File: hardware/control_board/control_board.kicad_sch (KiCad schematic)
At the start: 32 parts, among them J1 SWD, J2 Aux, J3 Panel, SW1 Reset, U1 STM32F103C8T6, Y1 8MHz

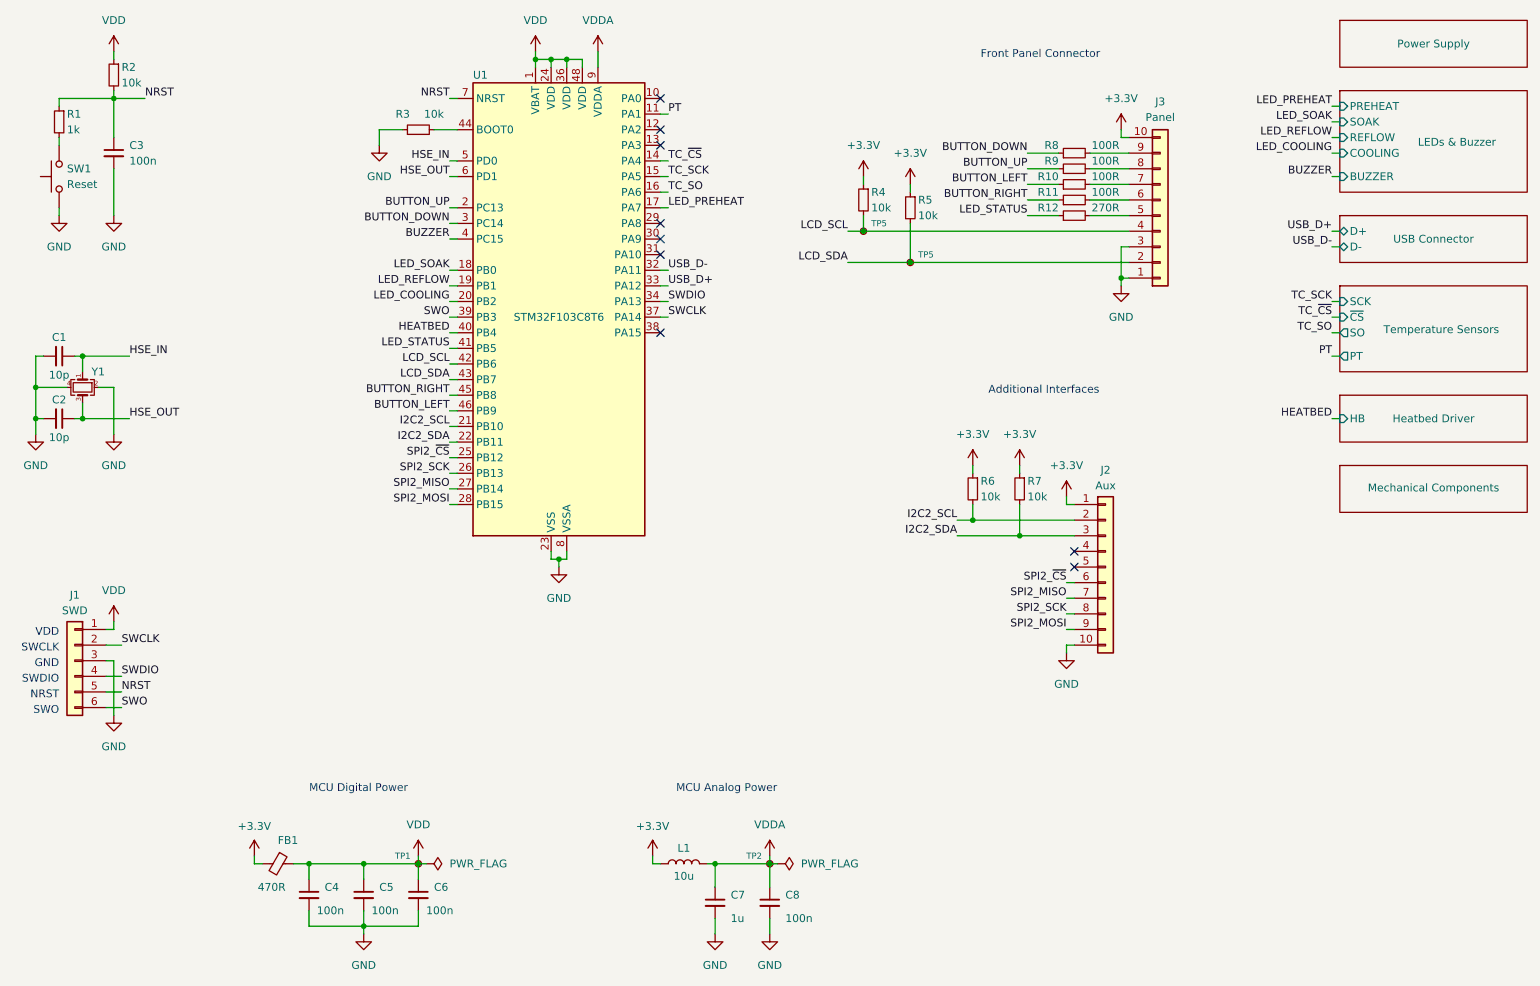
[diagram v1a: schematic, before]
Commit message: Change the buzzer
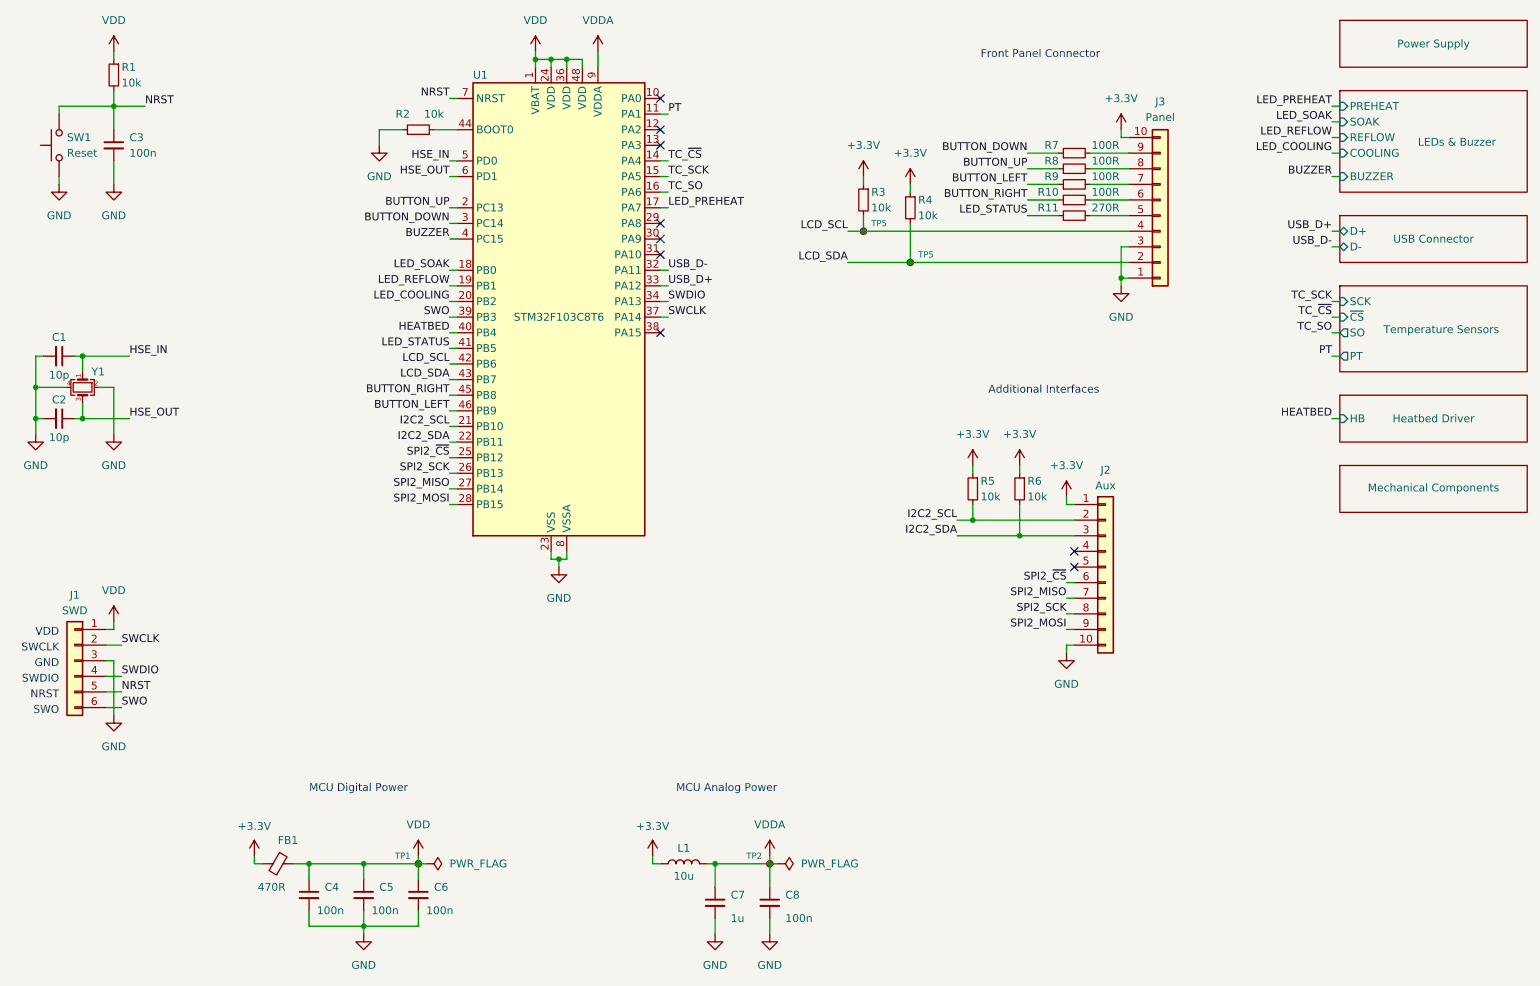
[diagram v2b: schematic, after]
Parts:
- removed R1: 1k, Resistor_SMD:R_0603_1608Metric, symbol Device:R_Small
- renumbered R2 to R1, R11 to R10, R12 to R11, R3 to R2, R4 to R3, R5 to R4, R6 to R5, R7 to R6, R8 to R7, R9 to R8, R10 to R9
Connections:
- net NRST: now also SW1.2
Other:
- moved on the sheet: C3, SW1

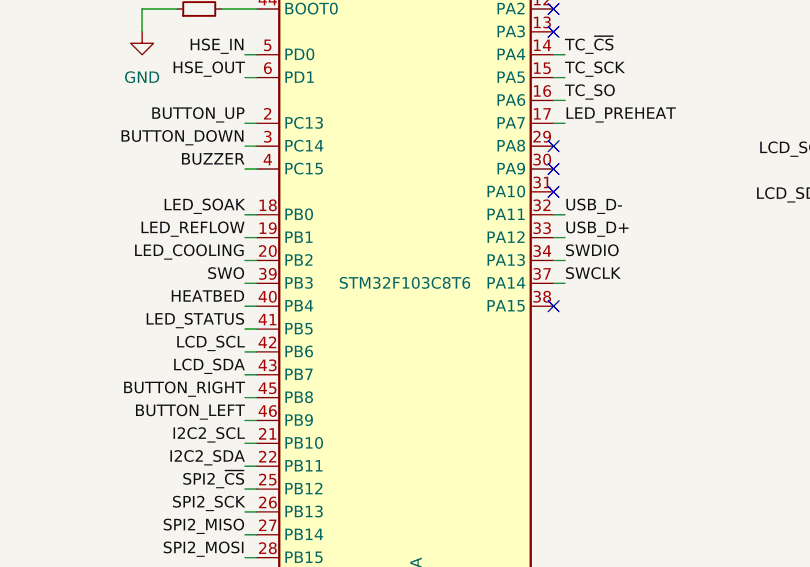
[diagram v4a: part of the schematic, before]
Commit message: Change MCU to STM32F103CBT6
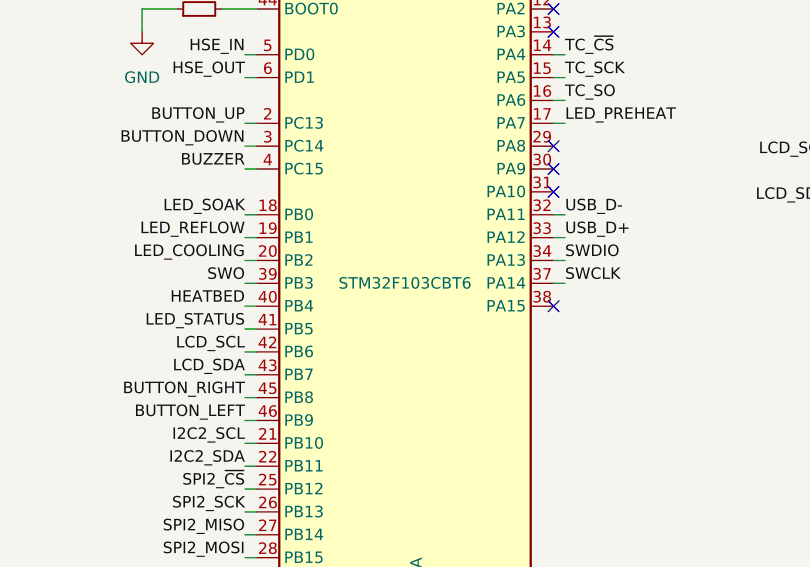
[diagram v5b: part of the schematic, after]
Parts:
- U1: value STM32F103C8T6 -> STM32F103CBT6
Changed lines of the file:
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@@
       (effects (font (size 1.27 1.27)) (justify left))
     )
-    (property "Value" "STM32F103C8T6" (at 114.3 78.74 0)
+    (property "Value" "STM32F103CBT6" (at 114.3 78.74 0)
       (effects (font (size 1.27 1.27)))
     )

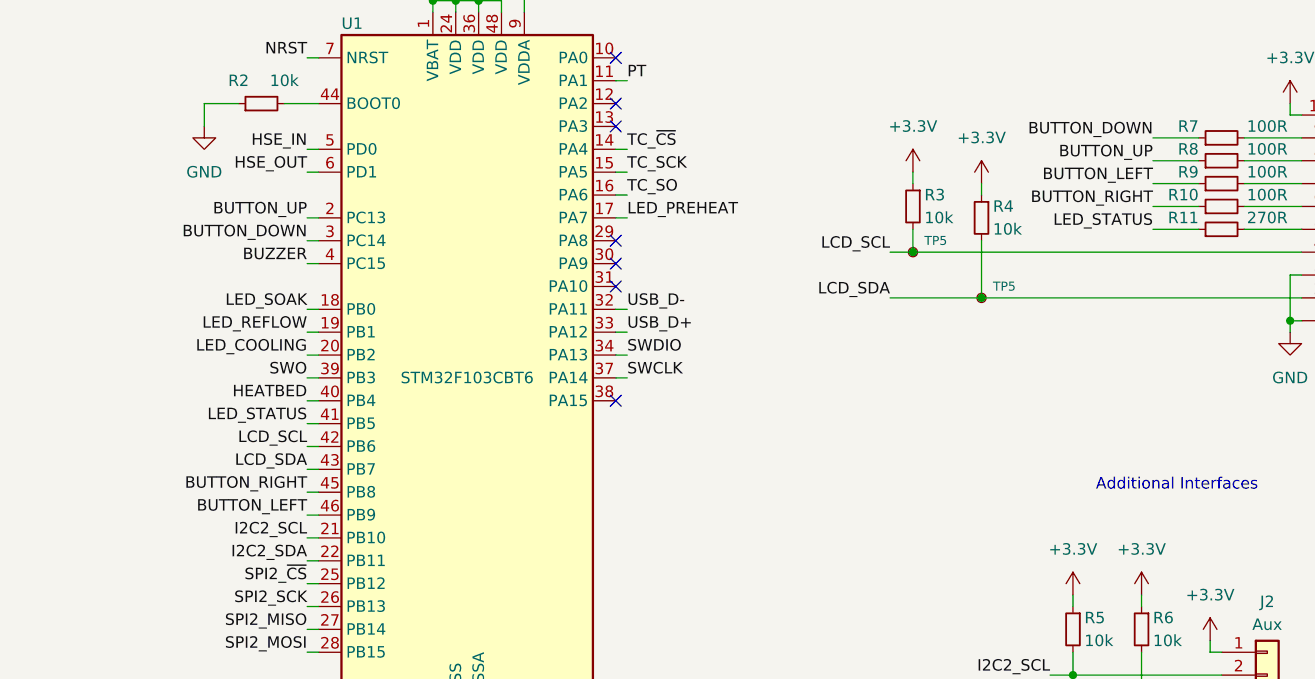
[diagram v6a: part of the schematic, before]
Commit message: Swap the left and right button signals
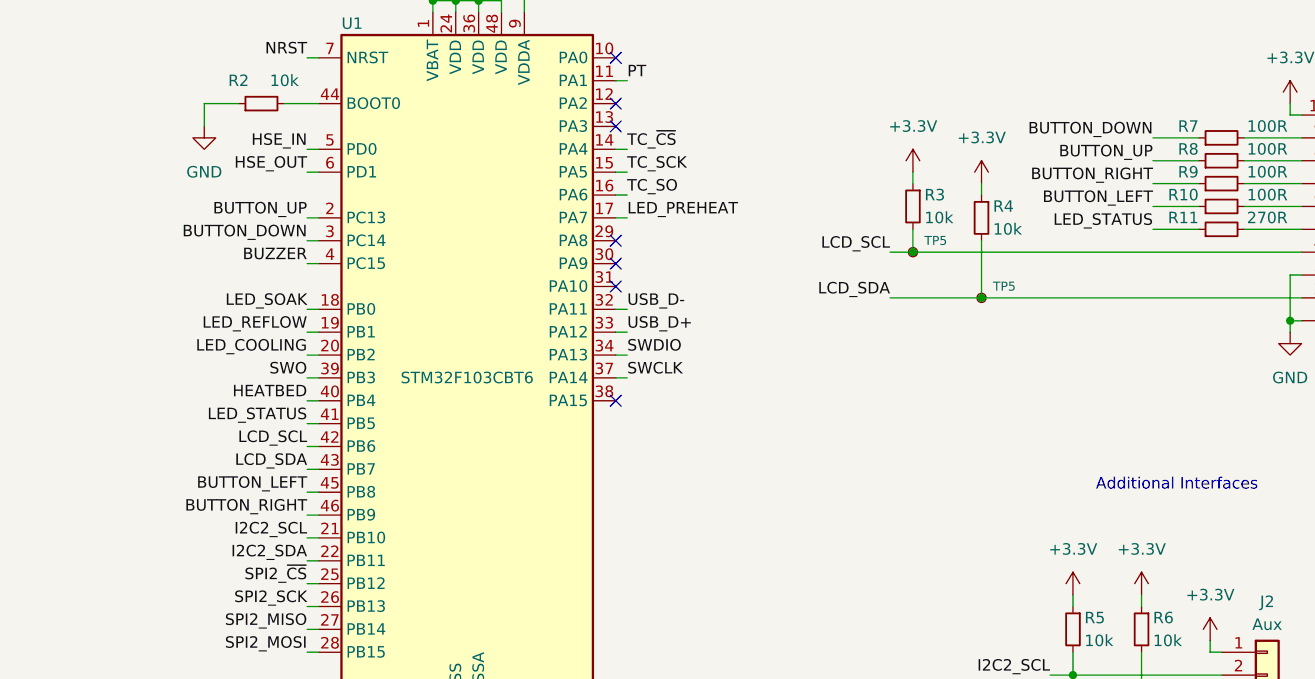
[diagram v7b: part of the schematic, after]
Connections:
- net BUTTON_LEFT: now also R10.1, U1.45 (PB8); no longer R9.1, U1.46 (PB9)
- net BUTTON_RIGHT: now also R9.1, U1.46 (PB9); no longer R10.1, U1.45 (PB8)
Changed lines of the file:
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@@
     (effects (font (size 1.27 1.27)) (justify right bottom))
   )
-  (label "BUTTON_LEFT" (at 190.5 57.15 180) (fields_autoplaced)
+  (label "BUTTON_LEFT" (at 190.5 59.69 180) (fields_autoplaced)
     (effects (font (size 1.27 1.27)) (justify right bottom))
   )
@@
     (effects (font (size 1.27 1.27)) (justify right bottom))
   )
-  (label "BUTTON_RIGHT" (at 96.52 91.44 180) (fields_autoplaced)
+  (label "BUTTON_RIGHT" (at 96.52 93.98 180) (fields_autoplaced)
     (effects (font (size 1.27 1.27)) (justify right bottom))
   )
@@
     (effects (font (size 1.27 1.27)) (justify left bottom))
   )
-  (label "BUTTON_RIGHT" (at 190.5 59.69 180) (fields_autoplaced)
+  (label "BUTTON_RIGHT" (at 190.5 57.15 180) (fields_autoplaced)
     (effects (font (size 1.27 1.27)) (justify right bottom))
   )
@@
     (effects (font (size 1.27 1.27)) (justify right bottom))
   )
-  (label "BUTTON_LEFT" (at 96.52 93.98 180) (fields_autoplaced)
+  (label "BUTTON_LEFT" (at 96.52 91.44 180) (fields_autoplaced)
     (effects (font (size 1.27 1.27)) (justify right bottom))
   )

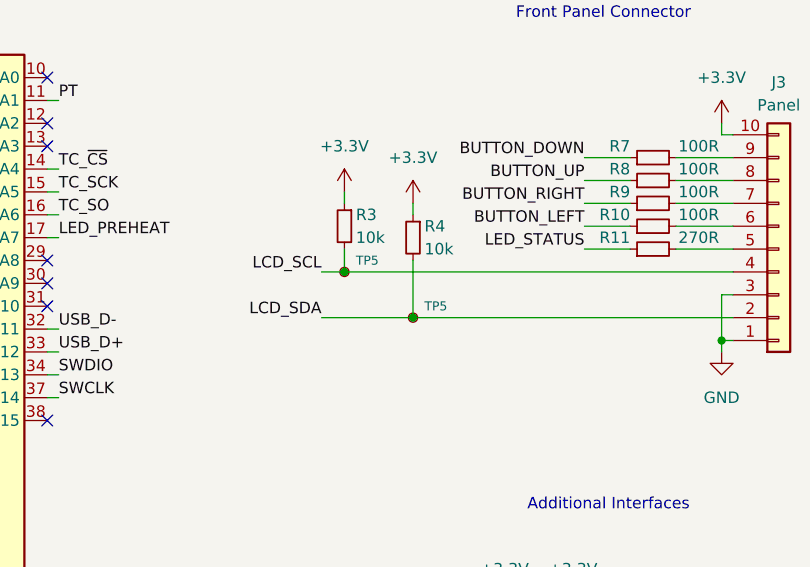
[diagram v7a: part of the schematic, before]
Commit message: Update reference designators
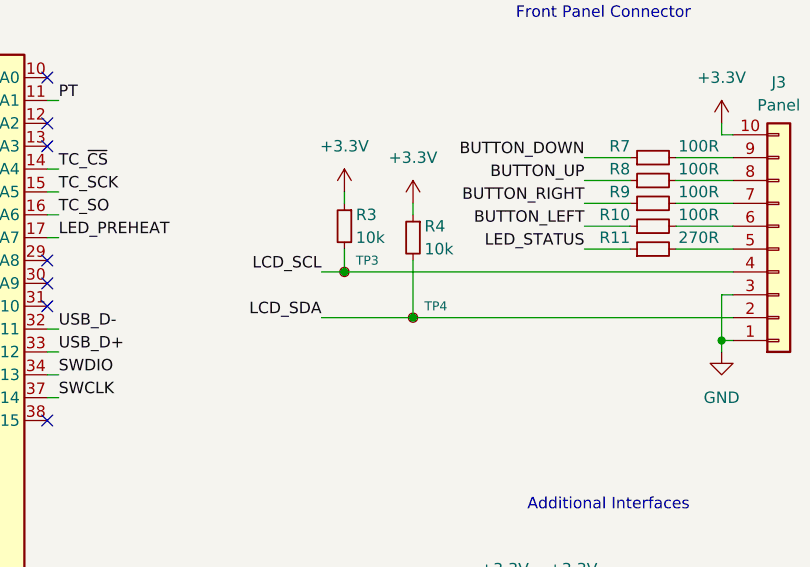
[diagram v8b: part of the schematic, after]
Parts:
- renumbered TP5 to TP3, TP5 to TP4
